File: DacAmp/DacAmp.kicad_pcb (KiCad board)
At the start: 2 copper layers, 105 parts, among them J1 AudioPlug3, J2 USB_B, U1 PCM2906C, U10 TLV70237_SOT23-5, U11 TLV61046ADB, U12 NE5532, U13 LM2941LD_NOPB, U2 NE5532, U3 NE5532, U4 NE5532, U5 NE5532, U6 NE5532, U7 NE5532, U8 NE5532, U9 NE5532, Y1 12MHz

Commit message: start some layout
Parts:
- moved TP4 206.2 mm to (257.0, 53.7)
- moved R35 197.5 mm to (257.7, 48.8), turned to -90 degrees
- moved R34 196.8 mm to (257.7, 51.2), turned to 90 degrees
- moved C37 195.6 mm to (261.3, 49.9), turned to 90 degrees
- moved C38 184.5 mm to (253.4, 52.7)
- moved U13 183.9 mm to (254.7, 49.8)
- moved TP1 181.9 mm to (233.3, 48.5)
- moved U10 167.3 mm to (232.1, 51.7)
- moved C22 161.7 mm to (234.9, 51.5), turned to -90 degrees
- moved TP2 159.3 mm to (210.6, 52.9)
- moved C21 156.1 mm to (229.4, 51.3), turned to -90 degrees
- moved L1 154.4 mm to (206.6, 45.6), turned to 180 degrees
- moved C26 150.2 mm to (206.6, 52.9), turned to 180 degrees
- moved U11 143.8 mm to (206.6, 49.3)
- moved R29 142.9 mm to (203.9, 49.8), turned to 90 degrees
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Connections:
- C11 pad 2: /Preamp/VOUTR -> /Codec/VOUTR
- C15 pad 2: /Preamp/VOUTL -> /Codec/VOUTL
- C18 pad 2: /Preamp/PREAMP_OUT_L -> /Output stage/PREAMP_OUT_L
- C25 pad 2: /Preamp/PREAMP_OUT_R -> /Output stage/PREAMP_OUT_R
- D1 pad 2: /USB/CONN_D- -> /Codec/CONN_D-
- D2 pad 2: /USB/CONN_D+ -> /Codec/CONN_D+
- J2 pad 2: /USB/CONN_D- -> /Codec/CONN_D-
- J2 pad 3: /USB/CONN_D+ -> /Codec/CONN_D+
- R21 pad 2: /Preamp/PREAMP_OUT_L -> /Output stage/PREAMP_OUT_L
- R28 pad 2: /Preamp/PREAMP_OUT_R -> /Output stage/PREAMP_OUT_R
- RV2 pad 3: /Preamp/PREAMP_OUT_R -> /Output stage/PREAMP_OUT_R
- RV2 pad 6: /Preamp/PREAMP_OUT_L -> /Output stage/PREAMP_OUT_L
- U3 pad 7: /Preamp/PREAMP_OUT_R -> /Output stage/PREAMP_OUT_R
- U7 pad 7: /Preamp/PREAMP_OUT_L -> /Output stage/PREAMP_OUT_L
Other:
- copper layers 2 -> 4

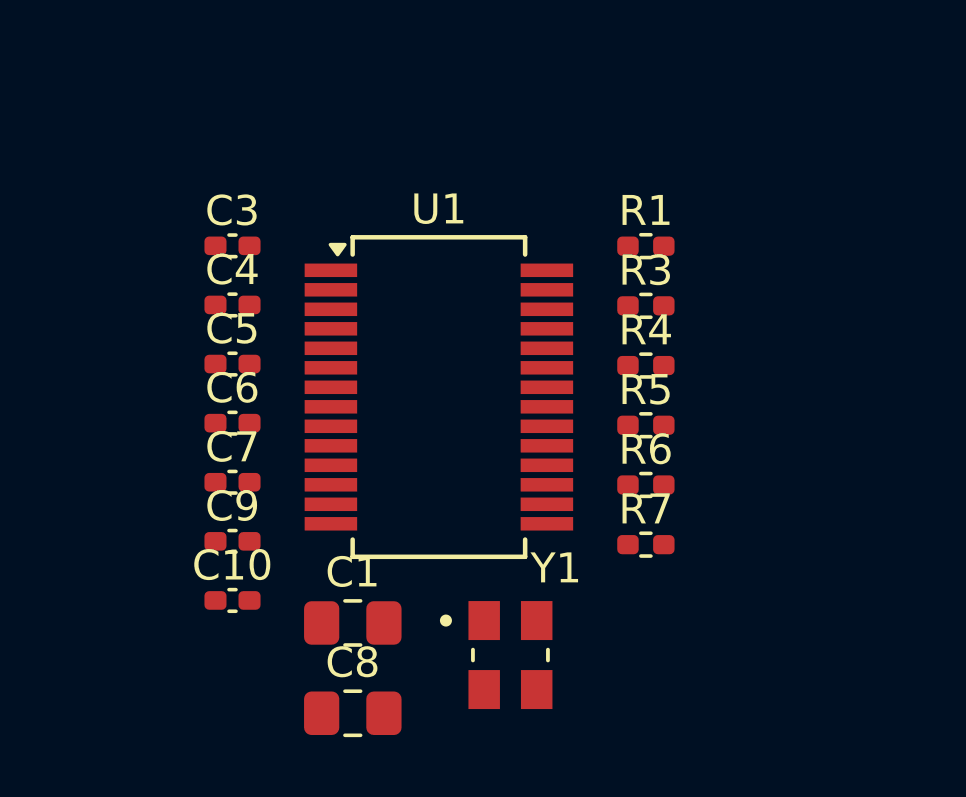
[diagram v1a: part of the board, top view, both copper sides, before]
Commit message: component placement for PCM
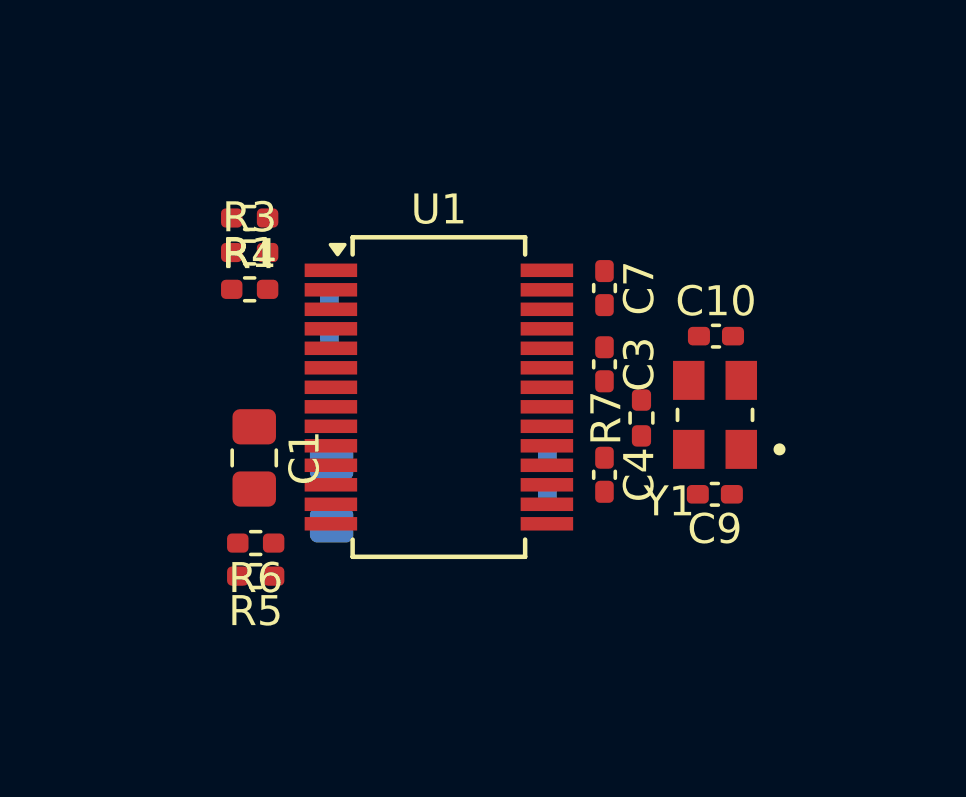
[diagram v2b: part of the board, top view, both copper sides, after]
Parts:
- C5, C6, C8: moved to B.Cu
- moved C10 18.4 mm to (73.9, 147.6)
- moved C9 16.2 mm to (73.8, 152.9), turned to 180 degrees
- moved C7 14.0 mm to (70.1, 146.0), turned to -90 degrees
- moved R5 13.9 mm to (58.5, 155.6), turned to 180 degrees
- moved C4 13.6 mm to (70.1, 152.2), turned to -90 degrees
- moved R4 13.5 mm to (58.3, 146.1)
- moved R3 13.3 mm to (58.3, 144.8)
- moved R1 13.2 mm to (58.3, 143.7), turned to 180 degrees
- moved R6 13.1 mm to (58.5, 154.5), turned to 180 degrees
- moved C3 13.0 mm to (70.1, 148.6), turned to -90 degrees
- moved C5 11.1 mm to (68.2, 152.2), turned to 90 degrees
- moved Y1 10.5 mm to (73.8, 150.2), turned to 180 degrees
- moved C8 7.35 mm to (61.1, 152.9), turned to 90 degrees
- moved C1 6.41 mm to (58.5, 151.7), turned to -90 degrees
- moved C6 4.79 mm to (61.0, 147.0), turned to -90 degrees
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
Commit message: component placement for op amps
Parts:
- added C39: 100n, Capacitor_SMD:C_0402_1005Metric_Pad0.74x0.62mm_HandSolder, F.Cu at (40.8, 58.5)
- added C40: 10n, Capacitor_SMD:C_0402_1005Metric_Pad0.74x0.62mm_HandSolder, F.Cu at (43.7, 58.5)
- added FB1: BLM18PG221SN1D, Inductor_SMD:L_0603_1608Metric_Pad1.05x0.95mm_HandSolder, F.Cu at (42.4, 56.8)
- added TP5: TestPoint, TestPoint:TestPoint_Pad_D1.5mm, F.Cu at (76.2, 60.3)
- added TP6: TestPoint, TestPoint:TestPoint_Pad_D1.5mm, F.Cu at (33.3, 53.5)
- moved C42 197.7 mm to (256.1, 101.5)
- moved C29 197.7 mm to (246.8, 95.9)
- moved C30 197.7 mm to (246.8, 98.9)
- moved R13 197.7 mm to (264.8, 93.4)
- moved R14 197.7 mm to (264.8, 95.9)
- moved R37 197.7 mm to (250.9, 97.4)
- moved R8 197.7 mm to (264.8, 88.4)
- moved R9 197.7 mm to (264.8, 90.9)
- moved U2 197.7 mm to (248.7, 71.5)
- moved U4 197.7 mm to (248.7, 78.0)
- moved D4 193.5 mm to (240.3, 121.2), turned to 90 degrees
- moved C26 191.7 mm to (20.8, 100.1)
- moved C37 191.7 mm to (75.5, 97.2)
- moved L1 191.7 mm to (20.8, 92.8)
- moved R27 191.7 mm to (17.4, 100.0)
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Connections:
- net Net-(U11-FB) renamed /Power/BST_FB
- net Net-(U11-SW) renamed /Power/SW
- net Net-(U12A-+) renamed /Power/7V5_IN
- net Net-(U12A--) renamed /Power/7V5_BUF1
- net Net-(U12B--) renamed /Power/7V5_BUF2

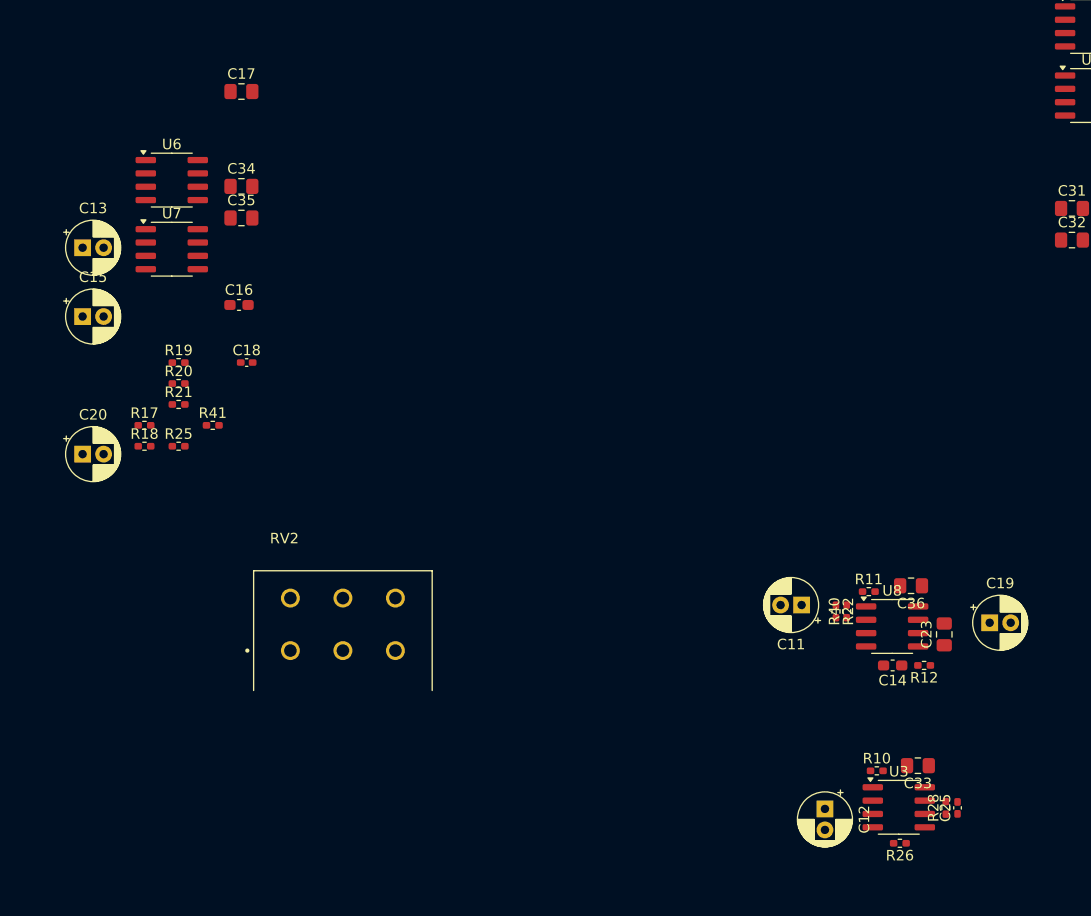
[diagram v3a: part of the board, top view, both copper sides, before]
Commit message: component placement of each preamp block
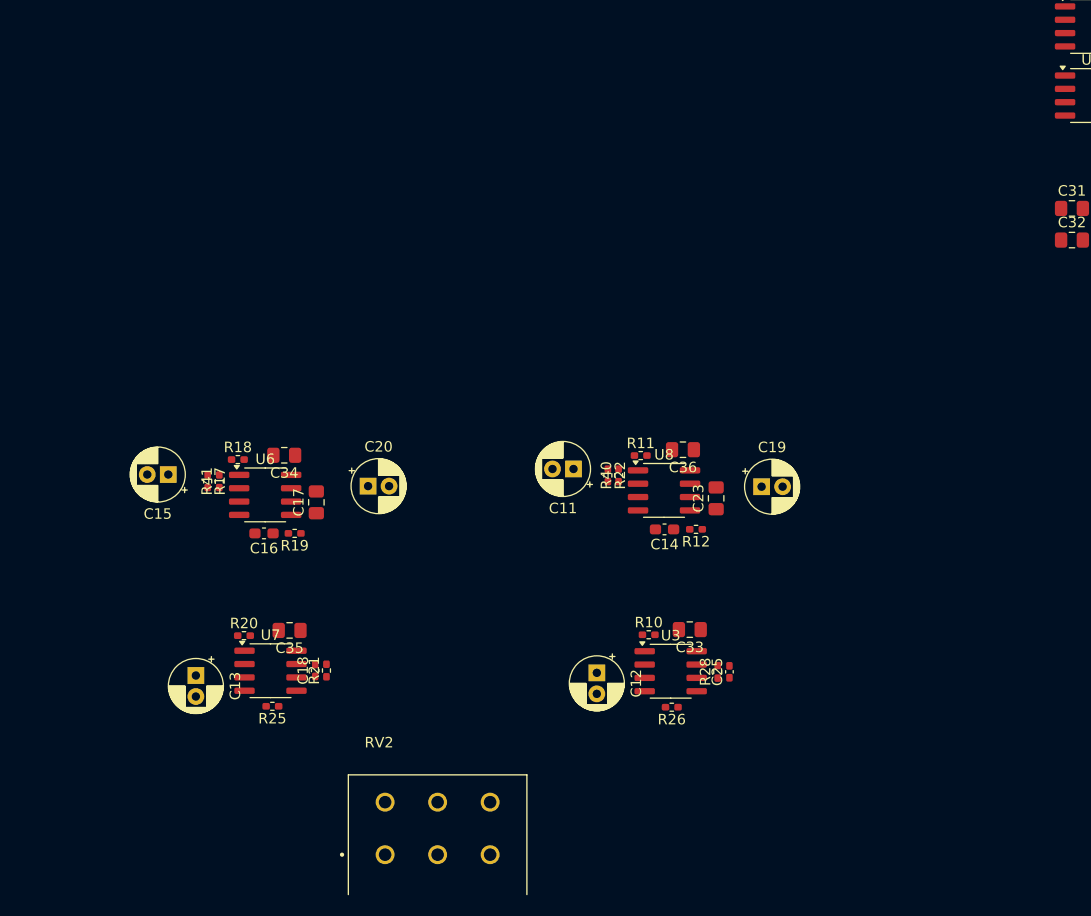
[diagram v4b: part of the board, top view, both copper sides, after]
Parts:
- moved C13 42.1 mm to (119.5, 135.4), turned to -90 degrees
- moved U7 41.2 mm to (126.6, 134.9)
- moved C17 39.8 mm to (131.0, 118.9), turned to 90 degrees
- moved C35 39.5 mm to (128.4, 131.1), turned to 180 degrees
- moved U6 31.3 mm to (126.1, 118.2)
- moved C18 30.0 mm to (130.8, 134.9), turned to 90 degrees
- moved R21 29.0 mm to (131.9, 134.9), turned to 90 degrees
- moved C20 27.3 mm to (135.9, 117.3)
- moved R25 26.3 mm to (126.8, 138.3), turned to 180 degrees
- moved C34 25.9 mm to (127.9, 114.4), turned to 180 degrees
- moved U3 25.3 mm to (164.7, 135.0)
- moved C19 25.3 mm to (173.3, 117.4)
- moved C23 25.3 mm to (169.0, 118.5)
- moved C36 25.3 mm to (165.9, 113.9)
- moved U8 25.3 mm to (164.1, 117.7)
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
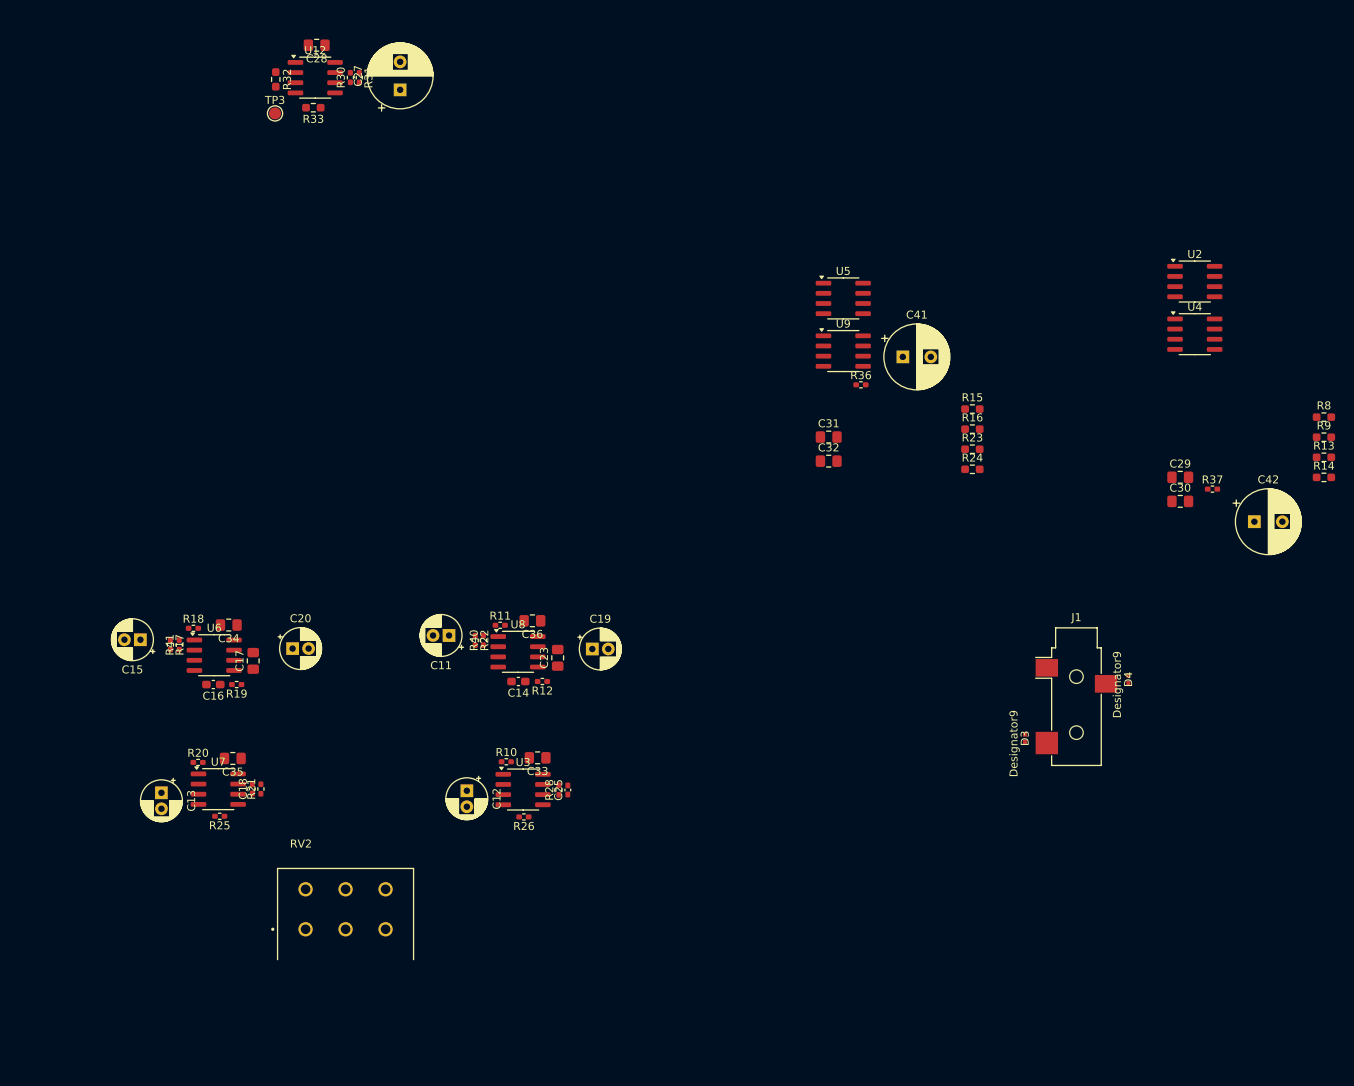
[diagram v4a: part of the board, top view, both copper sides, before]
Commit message: completed relative grouping of all blocks
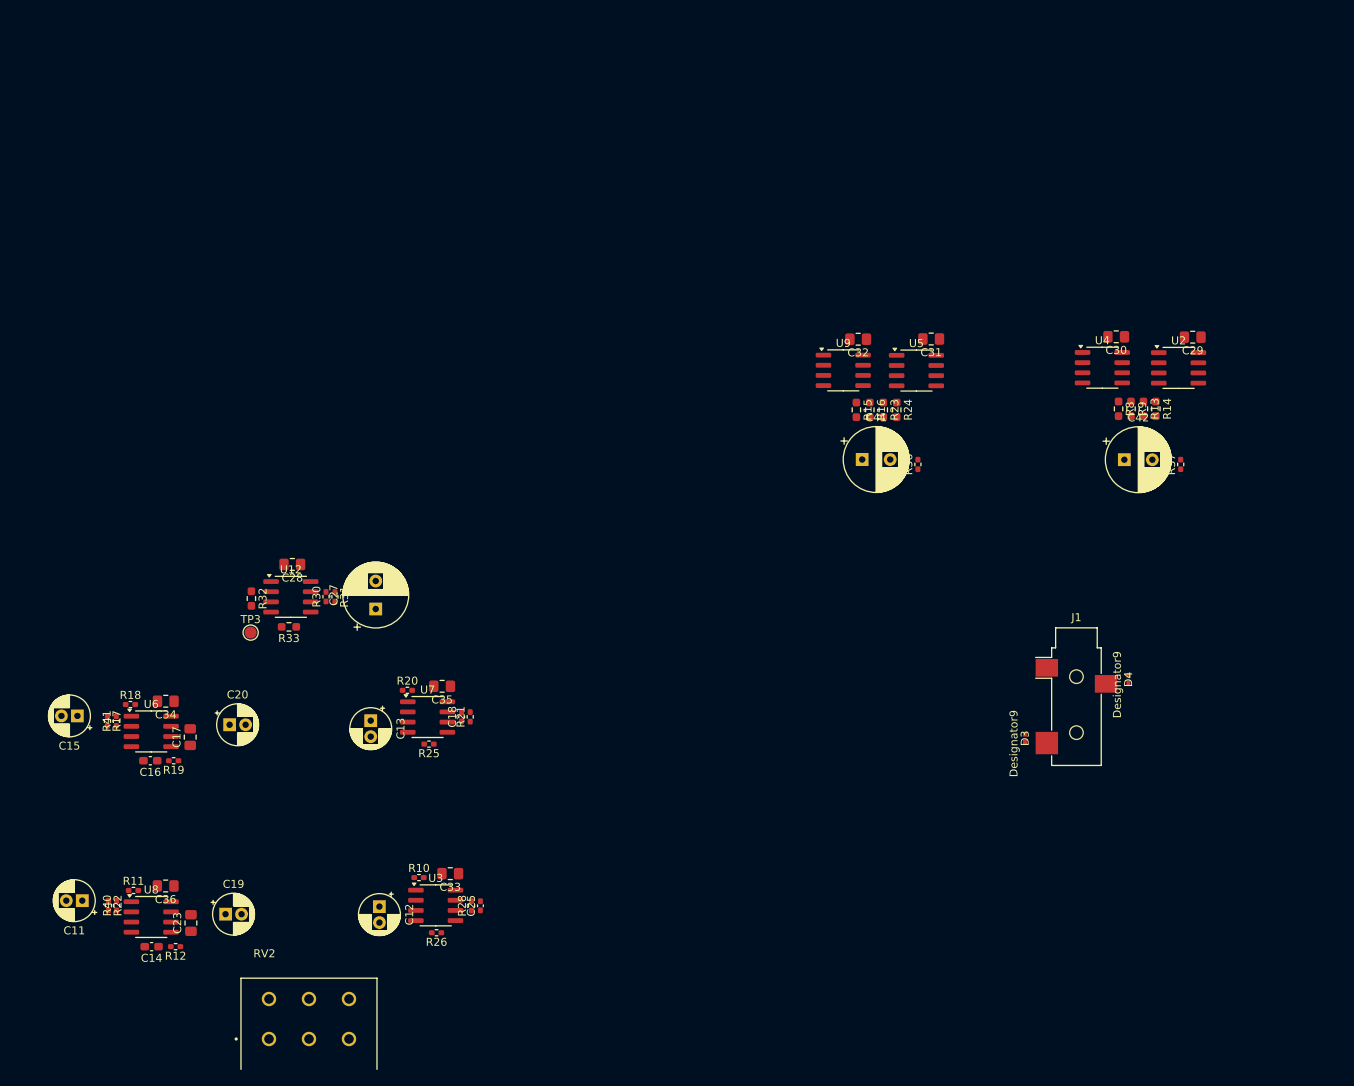
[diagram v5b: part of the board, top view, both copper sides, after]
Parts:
- moved R32 65.0 mm to (130.7, 111.1)
- moved C27 65.0 mm to (146.3, 112.4)
- moved C28 65.0 mm to (135.8, 106.8)
- moved R30 65.0 mm to (140.1, 110.9)
- moved R31 65.0 mm to (141.2, 110.9)
- moved R33 65.0 mm to (135.4, 114.6)
- moved TP3 65.0 mm to (130.6, 115.3)
- moved U12 65.0 mm to (135.7, 110.9)
- moved C11 56.6 mm to (109.6, 148.9)
- moved R11 56.6 mm to (116.0, 147.6)
- moved R12 56.6 mm to (121.3, 154.6)
- moved C14 56.6 mm to (118.3, 154.6)
- moved R22 56.6 mm to (112.9, 149.5)
- moved R40 56.6 mm to (113.9, 149.5)
- moved C19 56.6 mm to (127.5, 150.5)
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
